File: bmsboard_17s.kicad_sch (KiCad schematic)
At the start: 142 parts, among them J1 Conn_01x18, Q1 Q_NMOS_GDS, Q10 Q_NMOS_GDS, Q11 Q_NMOS_GDS, Q12 Q_PMOS_GDS, Q13 Q_NMOS_GDS, Q14 Q_NMOS_GDS, Q15 Q_NMOS_GDS, Q16 Q_NMOS_GDS, Q17 Q_NMOS_GDS, Q18 Q_NMOS_GDS, Q19 Q_NMOS_GDS, Q2 Q_NMOS_GDS, Q20 Q_NMOS_GDS, Q21 Q_NPN_BCE, Q3 Q_NMOS_GDS, Q4 Q_NMOS_GDS, Q5 Q_NMOS_GDS, Q6 Q_NMOS_GDS, Q7 Q_NMOS_GDS, Q8 Q_NMOS_GDS, Q9 Q_NMOS_GDS, U1 PB7170

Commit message: 为元器件分配封装，PCB上对元器件大致布局
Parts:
- C1, C10, C11, C12, C13, C14, C15, C16, C17, C18, C19, C2, C20, C21, C22, C23, C24, C25, C26, C27, C28, C29, C3, C4, C5, C6, C7, C8, C9: footprint (none) -> Capacitor_SMD:C_0603_1608Metric
- D1, D10, D11, D12, D13, D14, D15, D16, D17, D18, D19, D2, D20, D21, D22, D23, D24, D25, D26, D27, D28, D29, D3, D30, D4, D5, D6, D7, D8, D9: footprint (none) -> Diode_SMD:D_SOD-323
- Q1, Q2: footprint (none) -> Package_TO_SOT_SMD:TO-252-2
- Q10, Q11, Q12, Q13, Q14, Q15, Q16, Q17, Q18, Q19, Q20, Q21, Q3, Q4, Q5, Q6, Q7, Q8, Q9: footprint (none) -> Package_TO_SOT_SMD:SOT-23
- R1: footprint (none) -> Resistor_SMD:R_2512_6332Metric
- R10, R11, R12, R13, R14, R15, R16, R17, R18, R19, R2, R21, R22, R23, R24, R25, R26, R27, R28, R29, R3, R30, R31, R32, R33, R34, R36, R37, R38, R39, R4, R40, R41, R42, R43, R45, R46, R47, R49, R5, R50, R59, R6, R60, R7, R8, R9: footprint (none) -> Resistor_SMD:R_0603_1608Metric
- R20, R35, R44, R48, R51, R52, R53, R54, R55, R56, R57, R58: footprint (none) -> Resistor_SMD:R_0402_1005Metric

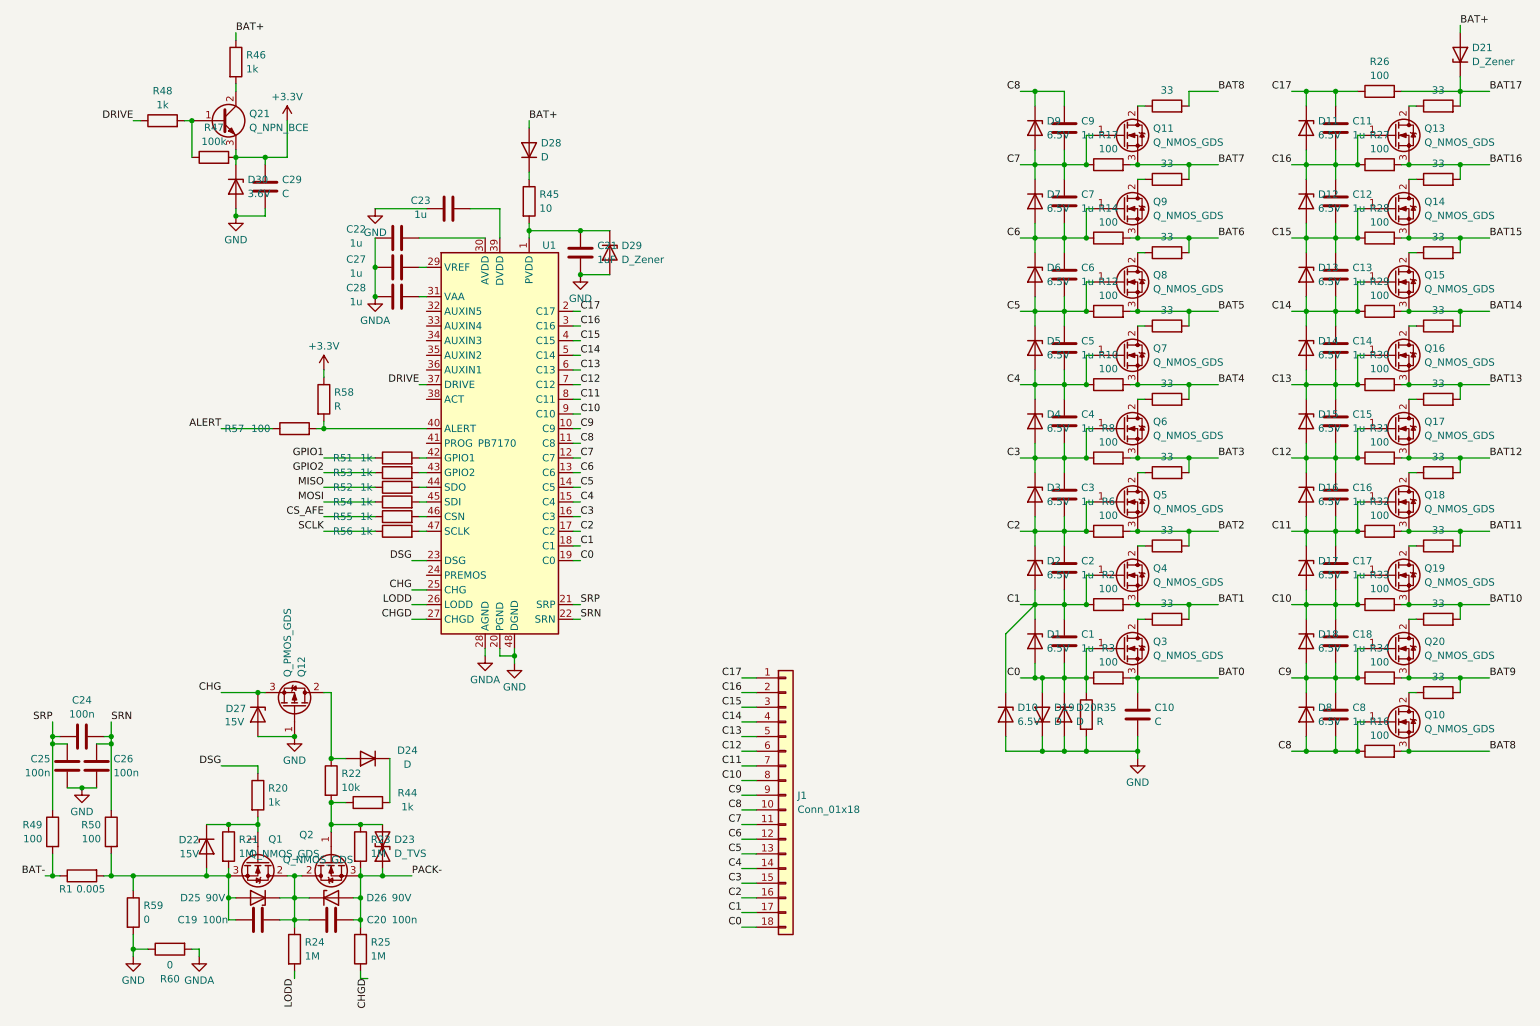
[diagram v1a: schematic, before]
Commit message: 重新分配位号，使电压采样电路的位号连续
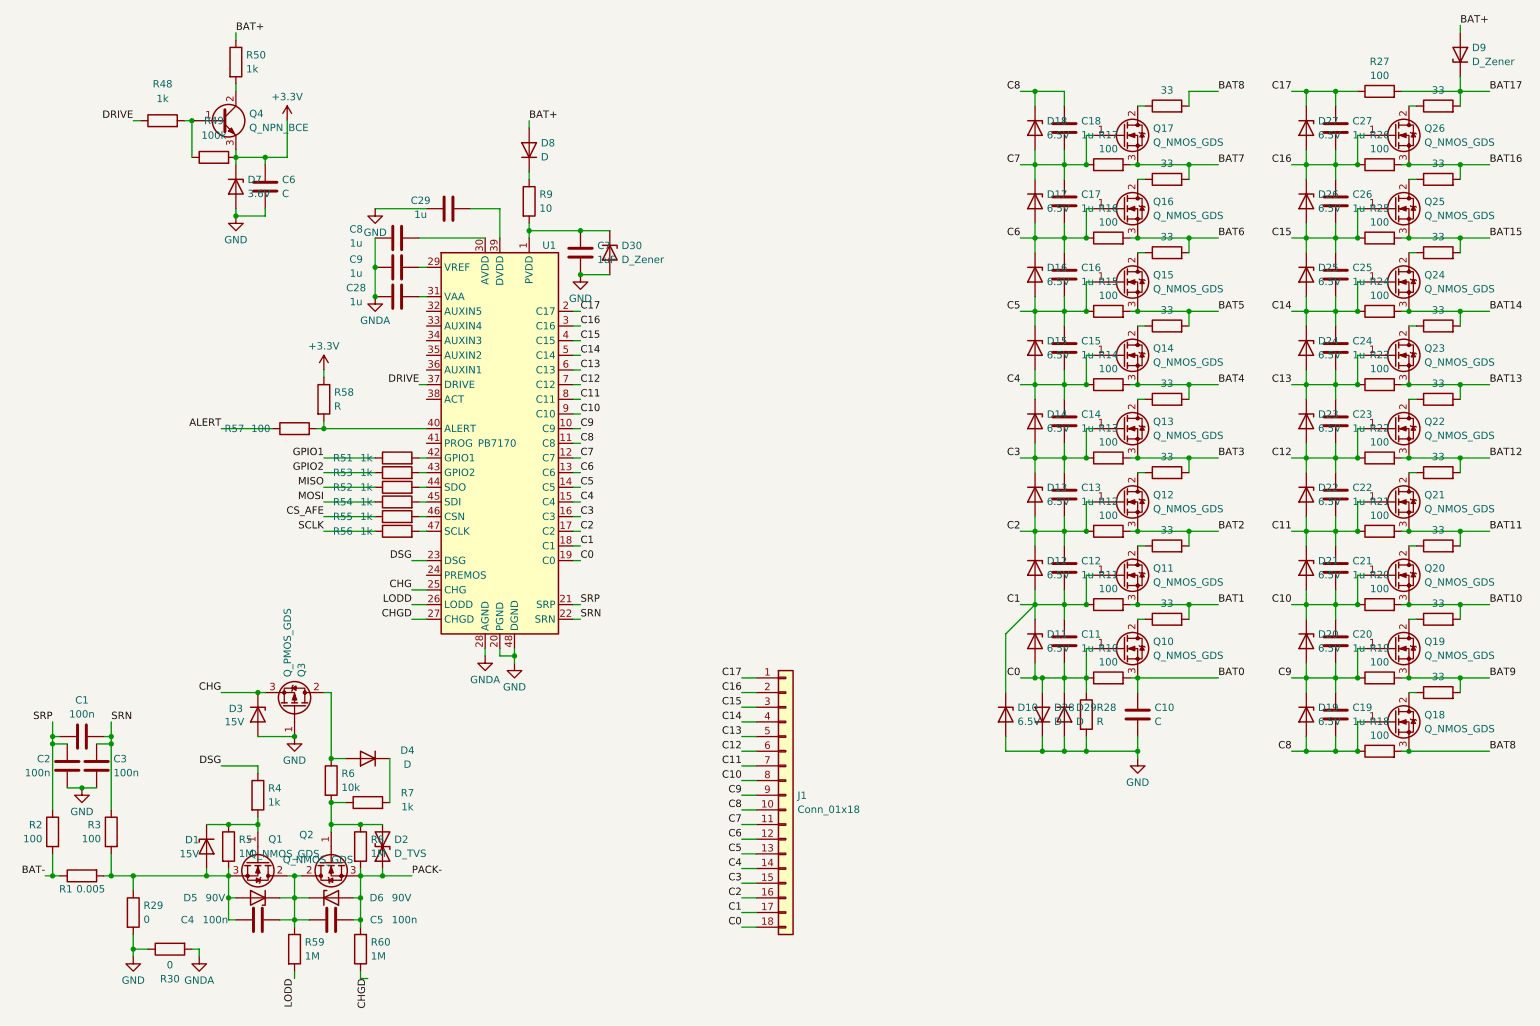
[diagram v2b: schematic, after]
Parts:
- renumbered C24 to C1, C1 to C11, C2 to C12, C3 to C13, C4 to C14, C5 to C15, C6 to C16, C7 to C17, C9 to C18, C8 to C19, C25 to C2, C18 to C20, C17 to C21, C16 to C22, C15 to C23, C14 to C24, C13 to C25, C12 to C26, C11 to C27, C23 to C29, C26 to C3, C19 to C4, C20 to C5, C29 to C6, C21 to C7, C22 to C8, C27 to C9, D22 to D1, D1 to D11, D2 to D12, D3 to D13, D4 to D14, D5 to D15, D6 to D16, D7 to D17, D9 to D18, D8 to D19, D23 to D2, D18 to D20, D17 to D21, D16 to D22, D15 to D23, D14 to D24, D13 to D25, D12 to D26, D11 to D27, D19 to D28, D20 to D29, D27 to D3, D29 to D30, D24 to D4, D25 to D5, D26 to D6, D30 to D7, D28 to D8, D21 to D9, Q3 to Q10, Q4 to Q11, Q5 to Q12, Q6 to Q13, Q7 to Q14, Q8 to Q15, Q9 to Q16, Q11 to Q17, Q10 to Q18, Q20 to Q19, Q19 to Q20, Q18 to Q21, Q17 to Q22, Q16 to Q23, Q15 to Q24, Q14 to Q25, Q13 to Q26, Q12 to Q3, Q21 to Q4, R3 to R10, R2 to R11, R6 to R12, R8 to R13, R10 to R14, R12 to R15, R14 to R16, R16 to R18, R34 to R19, R49 to R2, R33 to R20, R32 to R21, R31 to R22, R30 to R23, R29 to R24, R28 to R25, R27 to R26, R26 to R27, R35 to R28, R59 to R29, R50 to R3, R60 to R30, R4 to R31, R5 to R32, R7 to R33, R9 to R34, R11 to R35, R13 to R36, R15 to R37, R19 to R38, R18 to R39, R20 to R4, R43 to R40, R42 to R41, R41 to R42, R40 to R43, R39 to R44, R38 to R45, R37 to R46, R36 to R47, R47 to R49, R21 to R5, R46 to R50, R24 to R59, R22 to R6, R25 to R60, R44 to R7, R23 to R8, R45 to R9

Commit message: refactor: AFE相关电路移动到子目录
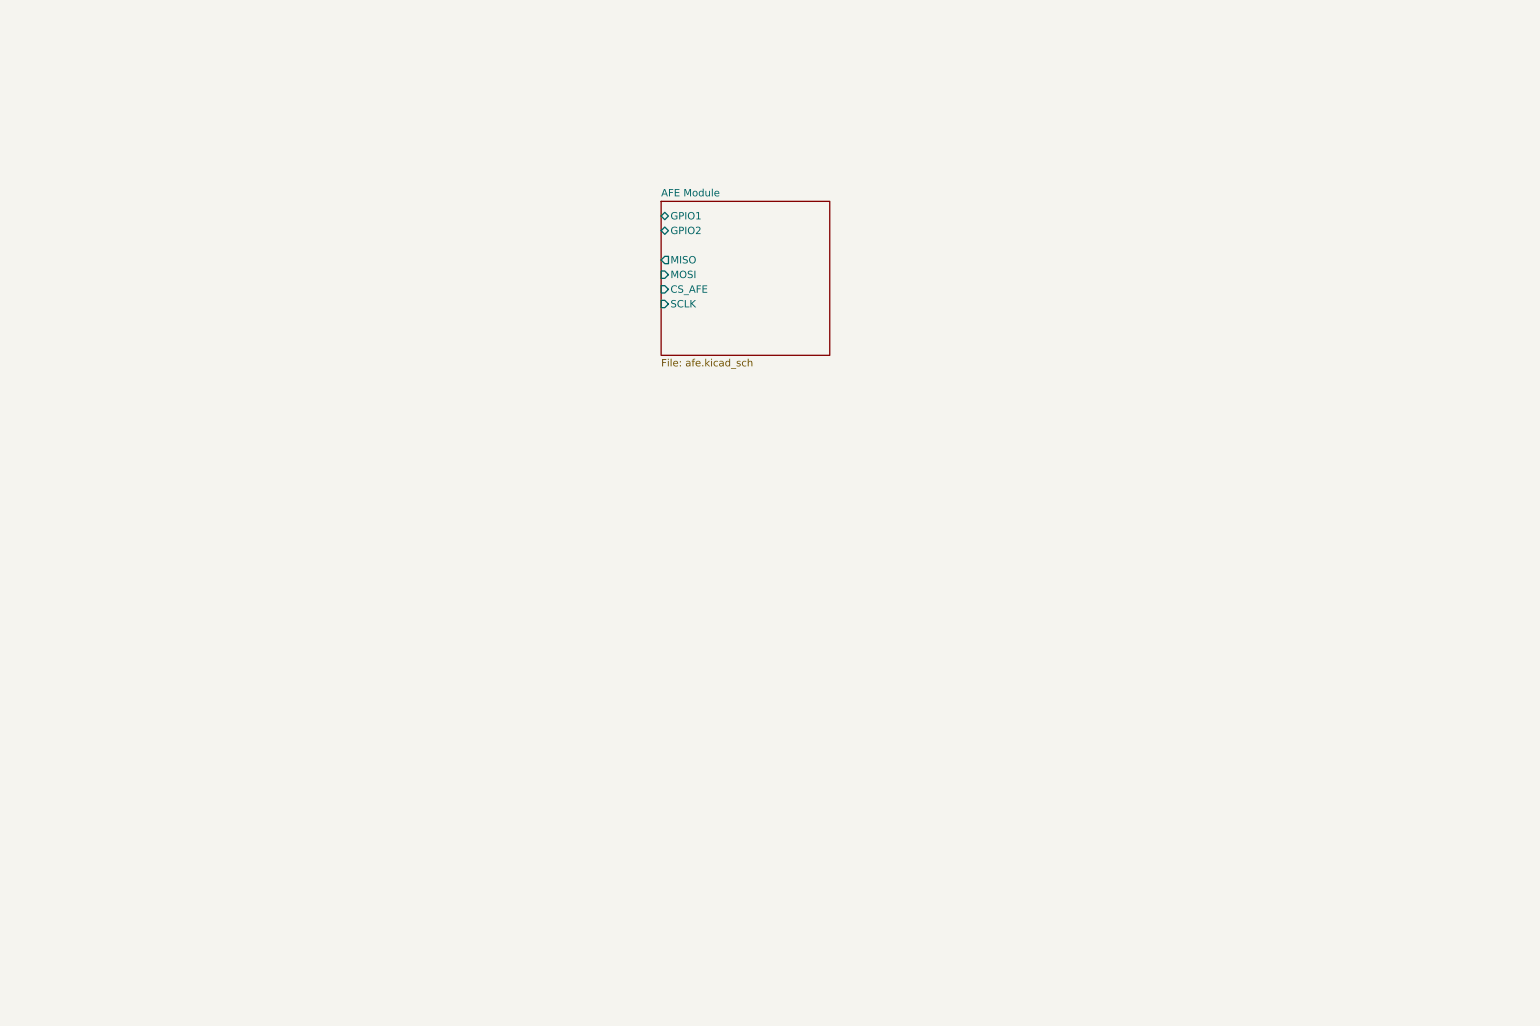
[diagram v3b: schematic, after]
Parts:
- removed C1, C2, C3, C4, C5: 100n, Capacitor_SMD:C_0603_1608Metric, symbol Device:C
- removed C10, C6: C, Capacitor_SMD:C_0603_1608Metric, symbol Device:C
- removed C11, C12, C13, C14, C15, C16, C17, C18, C19, C20, C21, C22, C23, C24, C25, C26, C27, C28, C29, C8, C9: 1u, Capacitor_SMD:C_0603_1608Metric, symbol Device:C
- removed C7: 1uF, Capacitor_SMD:C_0603_1608Metric, symbol Device:C
- removed D1, D3: 15V, Diode_SMD:D_SOD-323, symbol Device:D_Zener
- removed D10, D11, D12, D13, D14, D15, D16, D17, D18, D19, D20, D21, D22, D23, D24, D25, D26, D27: 6.5V, Diode_SMD:D_SOD-323, symbol Device:D_Zener
- removed D2: D_TVS, Diode_SMD:D_SOD-323, symbol Device:D_TVS
- removed D28, D29, D4, D8: D, Diode_SMD:D_SOD-323, symbol Device:D
- removed D30, D9: D_Zener, Diode_SMD:D_SOD-323, symbol Device:D_Zener
- removed D5, D6: 90V, Diode_SMD:D_SOD-323, symbol Device:D_Zener
- removed D7: 3.6V, Diode_SMD:D_SOD-323, symbol Device:D_Zener
- removed J1: Conn_01x18, symbol Connector_Generic:Conn_01x18
- removed Q1, Q2: Q_NMOS_GDS, Package_TO_SOT_SMD:TO-252-2, symbol Device:Q_NMOS_GDS
- removed Q10, Q11, Q12, Q13, Q14, Q15, Q16, Q17, Q18, Q19, Q20, Q21, Q22, Q23, Q24, Q25, Q26: Q_NMOS_GDS, Package_TO_SOT_SMD:SOT-23, symbol Device:Q_NMOS_GDS
- removed Q3: Q_PMOS_GDS, Package_TO_SOT_SMD:SOT-23, symbol Device:Q_PMOS_GDS
- removed Q4: Q_NPN_BCE, Package_TO_SOT_SMD:SOT-23, symbol Device:Q_NPN_BCE
- removed R1: 0.005, Resistor_SMD:R_2512_6332Metric, symbol Device:R
- removed R10, R11, R12, R13, R14, R15, R16, R17, R18, R19, R2, R20, R21, R22, R23, R24, R25, R26, R27, R3: 100, Resistor_SMD:R_0603_1608Metric, symbol Device:R
- removed R28, R58: R, Resistor_SMD:R_0402_1005Metric, symbol Device:R
- removed R29, R30: 0, Resistor_SMD:R_0603_1608Metric, symbol Device:R
- removed R31, R32, R33, R34, R35, R36, R37, R38, R39, R40, R41, R42, R43, R44, R45, R46, R47: 33, Resistor_SMD:R_0603_1608Metric, symbol Device:R
- removed R4, R48, R51, R52, R53, R54, R55, R56, R7: 1k, Resistor_SMD:R_0402_1005Metric, symbol Device:R
- removed R49: 100k, Resistor_SMD:R_0603_1608Metric, symbol Device:R
- removed R5, R59, R60, R8: 1M, Resistor_SMD:R_0603_1608Metric, symbol Device:R
- removed R50: 1k, Resistor_SMD:R_0603_1608Metric, symbol Device:R
- removed R57: 100, Resistor_SMD:R_0402_1005Metric, symbol Device:R
- removed R6: 10k, Resistor_SMD:R_0603_1608Metric, symbol Device:R
- removed R9: 10, Resistor_SMD:R_0603_1608Metric, symbol Device:R
- removed U1: PB7170, Package_QFP:LQFP-48-1EP_7x7mm_P0.5mm_EP3.6x3.6mm_ThermalVias, symbol project_symbols:PB7170
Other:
- added sheet AFE Module (afe.kicad_sch)

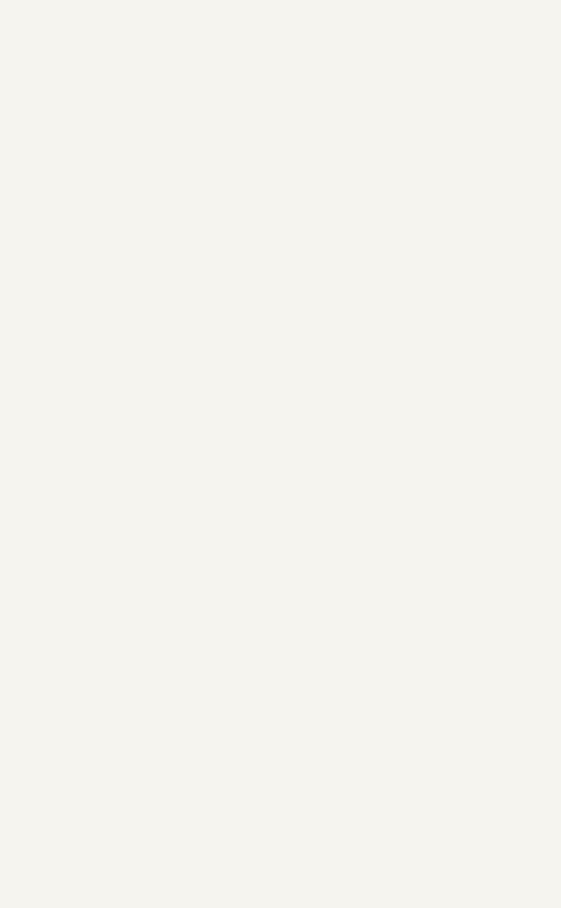
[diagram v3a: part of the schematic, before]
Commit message: 粗略绘制MCU和传感器相关原理图
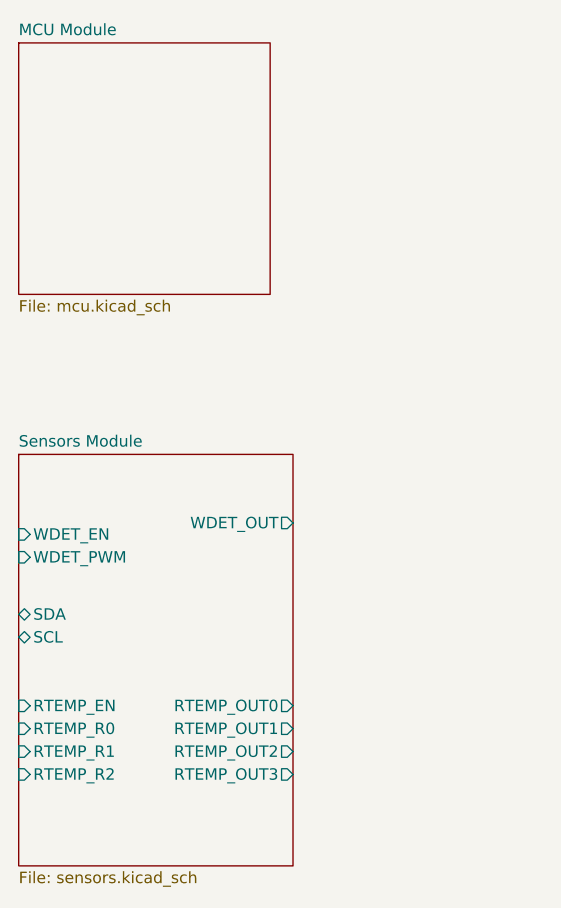
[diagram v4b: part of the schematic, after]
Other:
- added sheet MCU Module (mcu.kicad_sch)
- added sheet Sensors Module (sensors.kicad_sch)
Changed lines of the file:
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@@
+		)
+	)
+	(sheet
+		(at 50.8 97.79)
+		(size 30.48 45.72)
+		(fields_autoplaced yes)
+		(stroke
+			(width 0.1524)
+			(type solid)
+		)
+		(fill
+			(color 0 0 0 0.0000)
+		)
+		(property "Sheetname" "Sensors Module"
+			(at 50.8 97.0784 0)
+			(effects
+				(font
+					(size 1.27 1.27)
+				)
+				(justify left bottom)
+			)
+		)
+		(property "Sheetfile" "sensors.kicad_sch"
+			(at 50.8 144.0946 0)
+			(effects
+				(font
+					(size 1.27 1.27)
+				)
+				(justify left top)
+			)
+		)
+		(pin "WDET_EN" input
+			(at 50.8 106.68 180)
+			(effects
+				(font
+					(size 1.27 1.27)
+				)
+				(justify left)
+			)
+		)
+		(pin "SDA" bidirectional
+			(at 50.8 115.57 180)
+			(effects
+				(font
+					(size 1.27 1.27)
+				)
+				(justify left)
+			)
+		)
+		(pin "SCL" bidirectional
+			(at 50.8 118.11 180)
+			(effects
+				(font
+					(size 1.27 1.27)
+				)
+				(justify left)
+			)
+		)
+		(pin "WDET_PWM" input
+			(at 50.8 109.22 180)
+			(effects
+				(font
+					(size 1.27 1.27)
+				)
+				(justify left)
+			)
+		)
+		(pin "WDET_OUT" output
+			(at 81.28 105.41 0)
+			(effects
+				(font
+					(size 1.27 1.27)
+				)
+				(justify right)
+			)
+		)
+		(pin "RTEMP_OUT2" output
+			(at 81.28 130.81 0)
+			(effects
+				(font
+					(size 1.27 1.27)
+				)
+				(justify right)
+			)
+		)
+		(pin "RTEMP_OUT3" output
+			(at 81.28 133.35 0)
+			(effects
+				(font
+					(size 1.27 1.27)
+				)
+				(justify right)
+			)
+		)
+		(pin "RTEMP_OUT0" output
+			(at 81.28 125.73 0)
+			(effects
+				(font
+					(size 1.27 1.27)
+				)
+				(justify right)
+			)
+		)
+		(pin "RTEMP_OUT1" output
+			(at 81.28 128.27 0)
+			(effects
+				(font
+					(size 1.27 1.27)
+				)
+				(justify right)
+			)
+		)
+		(pin "RTEMP_EN" input
+			(at 50.8 125.73 180)
+			(effects
+				(font
+					(size 1.27 1.27)
+				)
+				(justify left)
+			)
+		)
+		(pin "RTEMP_R2" input
+			(at 50.8 133.35 180)
+			(effects
+				(font
+					(size 1.27 1.27)
+				)
+				(justify left)
+			)
+		)
+		(pin "RTEMP_R0" input
+			(at 50.8 128.27 180)
+			(effects
+				(font
+					(size 1.27 1.27)
+				)
+				(justify left)
+			)
+		)
+		(pin "RTEMP_R1" input
+			(at 50.8 130.81 180)
+			(effects
+				(font
+					(size 1.27 1.27)
+				)
+				(justify left)
+			)
+		)
+		(instances
+			(project "bmsboard_17s"
+				(path "/8b3bc3d6-55f6-430e-b34e-509c7be416f4"
+					(page "4")
+				)
+			)
+		)
+	)
+	(sheet
+		(at 50.8 52.07)
+		(size 27.94 27.94)
+		(fields_autoplaced yes)
+		(stroke
+			(width 0.1524)
+			(type solid)
+		)
+		(fill
+			(color 0 0 0 0.0000)
+		)
+		(property "Sheetname" "MCU Module"
+			(at 50.8 51.3584 0)
+			(effects
+				(font
+					(size 1.27 1.27)
+				)
+				(justify left bottom)
+			)
+		)
+		(property "Sheetfile" "mcu.kicad_sch"
+			(at 50.8 80.5946 0)
+			(effects
+				(font
+					(size 1.27 1.27)
+				)
+				(justify left top)
+			)
+		)
+		(instances
+			(project "bmsboard_17s"
+				(path "/8b3bc3d6-55f6-430e-b34e-509c7be416f4"
+					(page "3")
+				)
+			)
 		)
 	)
